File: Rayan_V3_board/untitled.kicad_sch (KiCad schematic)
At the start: 3 parts, among them U1 TB6612FNG_C_8_EL, U2 TB6612FNG_C_8_EL, U3 TB6612FNG_C_8_EL

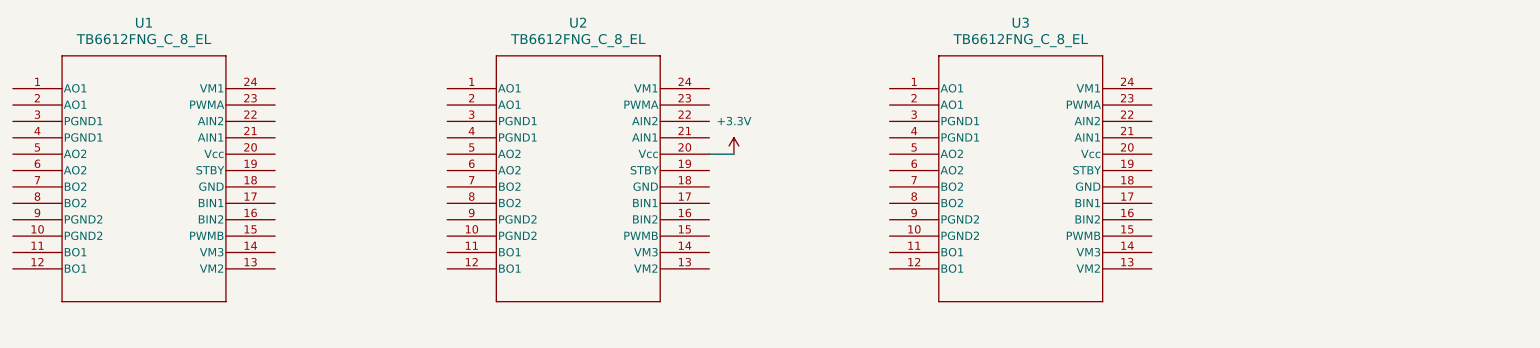
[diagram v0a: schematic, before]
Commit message: Created Motor Driver Schematics
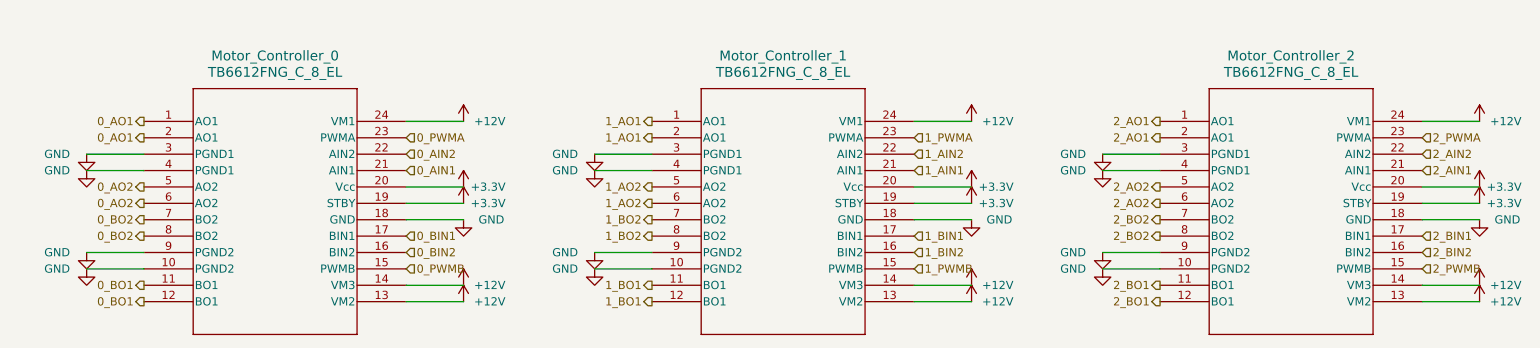
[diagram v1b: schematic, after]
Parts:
- removed U1, U3: TB6612FNG_C_8_EL, SSOP24-P-300-0p65A_TOS, symbol 2025-04-19_18-48-50:TB6612FNG_C_8_EL
- added Motor_Controller_0, Motor_Controller_2: TB6612FNG_C_8_EL, SSOP24-P-300-0p65A_TOS, symbol 2025-04-19_18-48-50:TB6612FNG_C_8_EL
- renumbered U2 to Motor_Controller_1
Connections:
- net +3.3V: now also Motor_Controller_1.19 (STBY), Motor_Controller_0.19 (STBY), Motor_Controller_0.20 (Vcc), Motor_Controller_2.19 (STBY), Motor_Controller_2.20 (Vcc)
- net 1_AO1: now reaches Motor_Controller_1.1 (AO1)
- net 1_AO1: now also Motor_Controller_1.2 (AO1)
- net GND: now reaches Motor_Controller_1.10 (PGND2)
- net GND: now also Motor_Controller_1.18 (GND), Motor_Controller_1.3 (PGND1), Motor_Controller_1.4 (PGND1), Motor_Controller_1.9 (PGND2), Motor_Controller_0.10 (PGND2), Motor_Controller_0.18 (GND), Motor_Controller_0.3 (PGND1), Motor_Controller_0.4 (PGND1), Motor_Controller_0.9 (PGND2), Motor_Controller_2.10 (PGND2), Motor_Controller_2.18 (GND), Motor_Controller_2.3 (PGND1), Motor_Controller_2.4 (PGND1), Motor_Controller_2.9 (PGND2)
- net 1_BO1: now reaches Motor_Controller_1.11 (BO1)
- net 1_BO1: now also Motor_Controller_1.12 (BO1)
- net +12V: now reaches Motor_Controller_1.13 (VM2)
- net +12V: now also Motor_Controller_1.14 (VM3), Motor_Controller_1.24 (VM1), Motor_Controller_0.13 (VM2), Motor_Controller_0.14 (VM3), Motor_Controller_0.24 (VM1), Motor_Controller_2.13 (VM2), Motor_Controller_2.14 (VM3), Motor_Controller_2.24 (VM1)
- net 1_PWMB: now reaches Motor_Controller_1.15 (PWMB)
- net 1_BIN2: now reaches Motor_Controller_1.16 (BIN2)
- net 1_BIN1: now reaches Motor_Controller_1.17 (BIN1)
- net 1_AIN1: now reaches Motor_Controller_1.21 (AIN1)
- net 1_AIN2: now reaches Motor_Controller_1.22 (AIN2)
- net 1_PWMA: now reaches Motor_Controller_1.23 (PWMA)
- net 1_AO2: now reaches Motor_Controller_1.5 (AO2)
- net 1_AO2: now also Motor_Controller_1.6 (AO2)
- net 1_BO2: now reaches Motor_Controller_1.7 (BO2)
- net 1_BO2: now also Motor_Controller_1.8 (BO2)
- new net 0_AIN1: Motor_Controller_0.21 (AIN1)
- new net 0_AIN2: Motor_Controller_0.22 (AIN2)
- new net 0_AO1: Motor_Controller_0.1 (AO1), Motor_Controller_0.2 (AO1)
- new net 0_AO2: Motor_Controller_0.5 (AO2), Motor_Controller_0.6 (AO2)
- new net 0_BIN1: Motor_Controller_0.17 (BIN1)
- new net 0_BIN2: Motor_Controller_0.16 (BIN2)
- new net 0_BO1: Motor_Controller_0.11 (BO1), Motor_Controller_0.12 (BO1)
- new net 0_BO2: Motor_Controller_0.7 (BO2), Motor_Controller_0.8 (BO2)
- new net 0_PWMA: Motor_Controller_0.23 (PWMA)
- new net 0_PWMB: Motor_Controller_0.15 (PWMB)
- new net 2_AIN1: Motor_Controller_2.21 (AIN1)
- new net 2_AIN2: Motor_Controller_2.22 (AIN2)
- new net 2_AO1: Motor_Controller_2.1 (AO1), Motor_Controller_2.2 (AO1)
- new net 2_AO2: Motor_Controller_2.5 (AO2), Motor_Controller_2.6 (AO2)
- new net 2_BIN1: Motor_Controller_2.17 (BIN1)
- new net 2_BIN2: Motor_Controller_2.16 (BIN2)
- new net 2_BO1: Motor_Controller_2.11 (BO1), Motor_Controller_2.12 (BO1)
- new net 2_BO2: Motor_Controller_2.7 (BO2), Motor_Controller_2.8 (BO2)
- new net 2_PWMA: Motor_Controller_2.23 (PWMA)
- new net 2_PWMB: Motor_Controller_2.15 (PWMB)
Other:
- title: (none) -> TB6612FNG Motor Drivers
- moved on the sheet: Motor_Controller_1
